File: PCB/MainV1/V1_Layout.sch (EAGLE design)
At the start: 48 parts, among them IC1 AD826N, IC3 AD623R, U2 MB85RC256VPF-G-JNERE2, X1 STEREOJACK

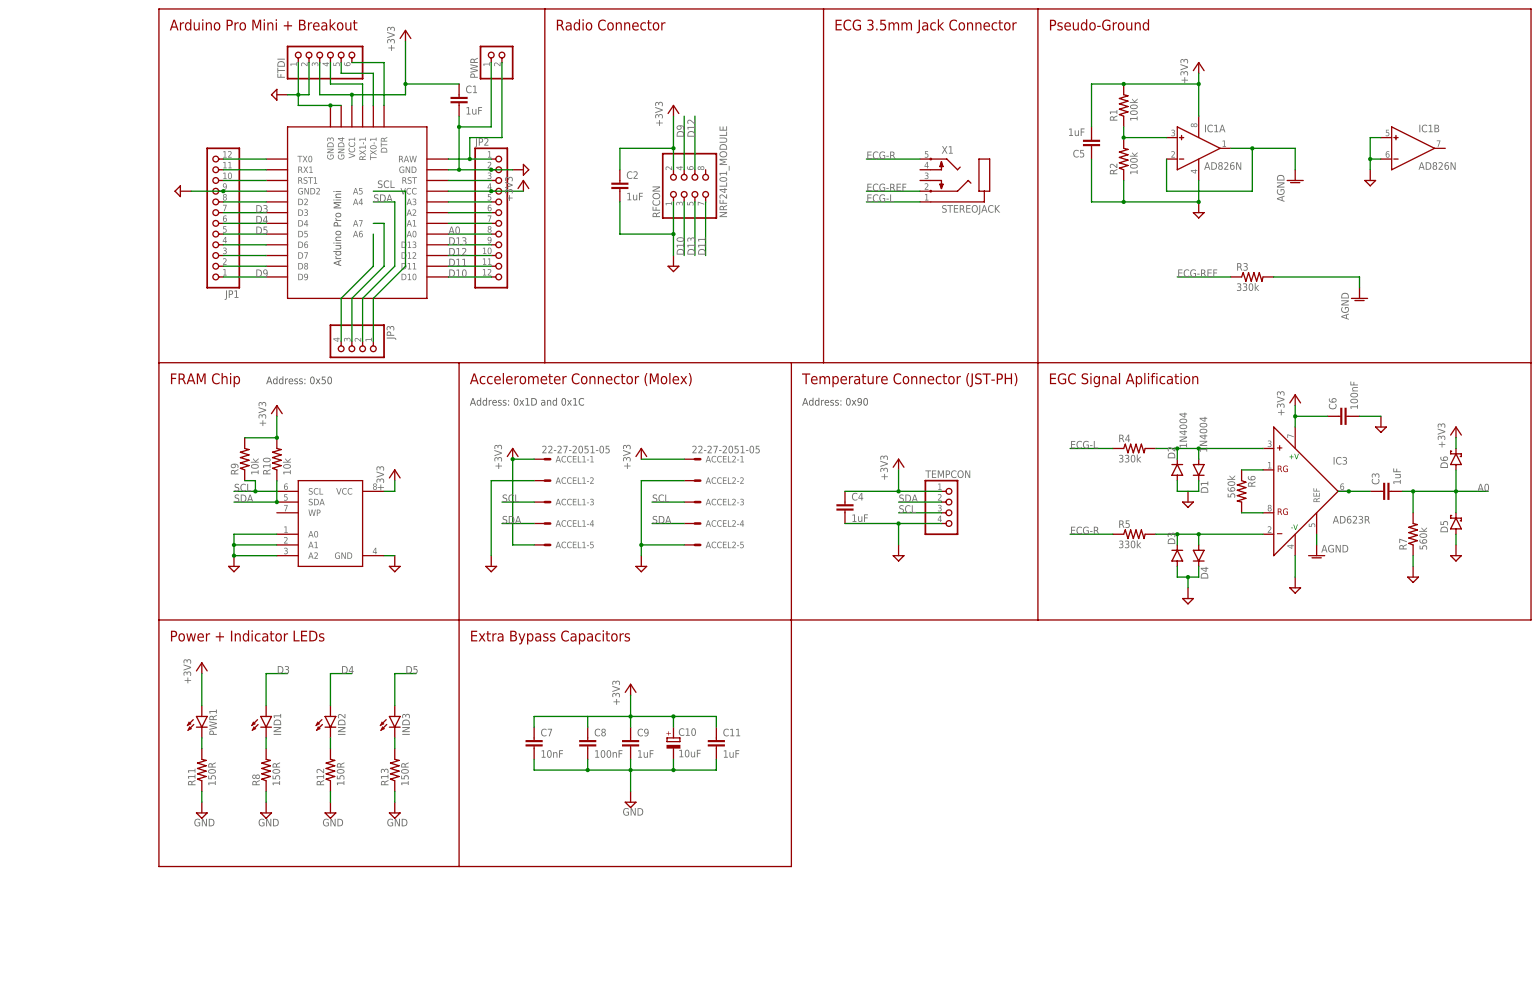
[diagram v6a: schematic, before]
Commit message: started initial main layout. Cleaned up files.
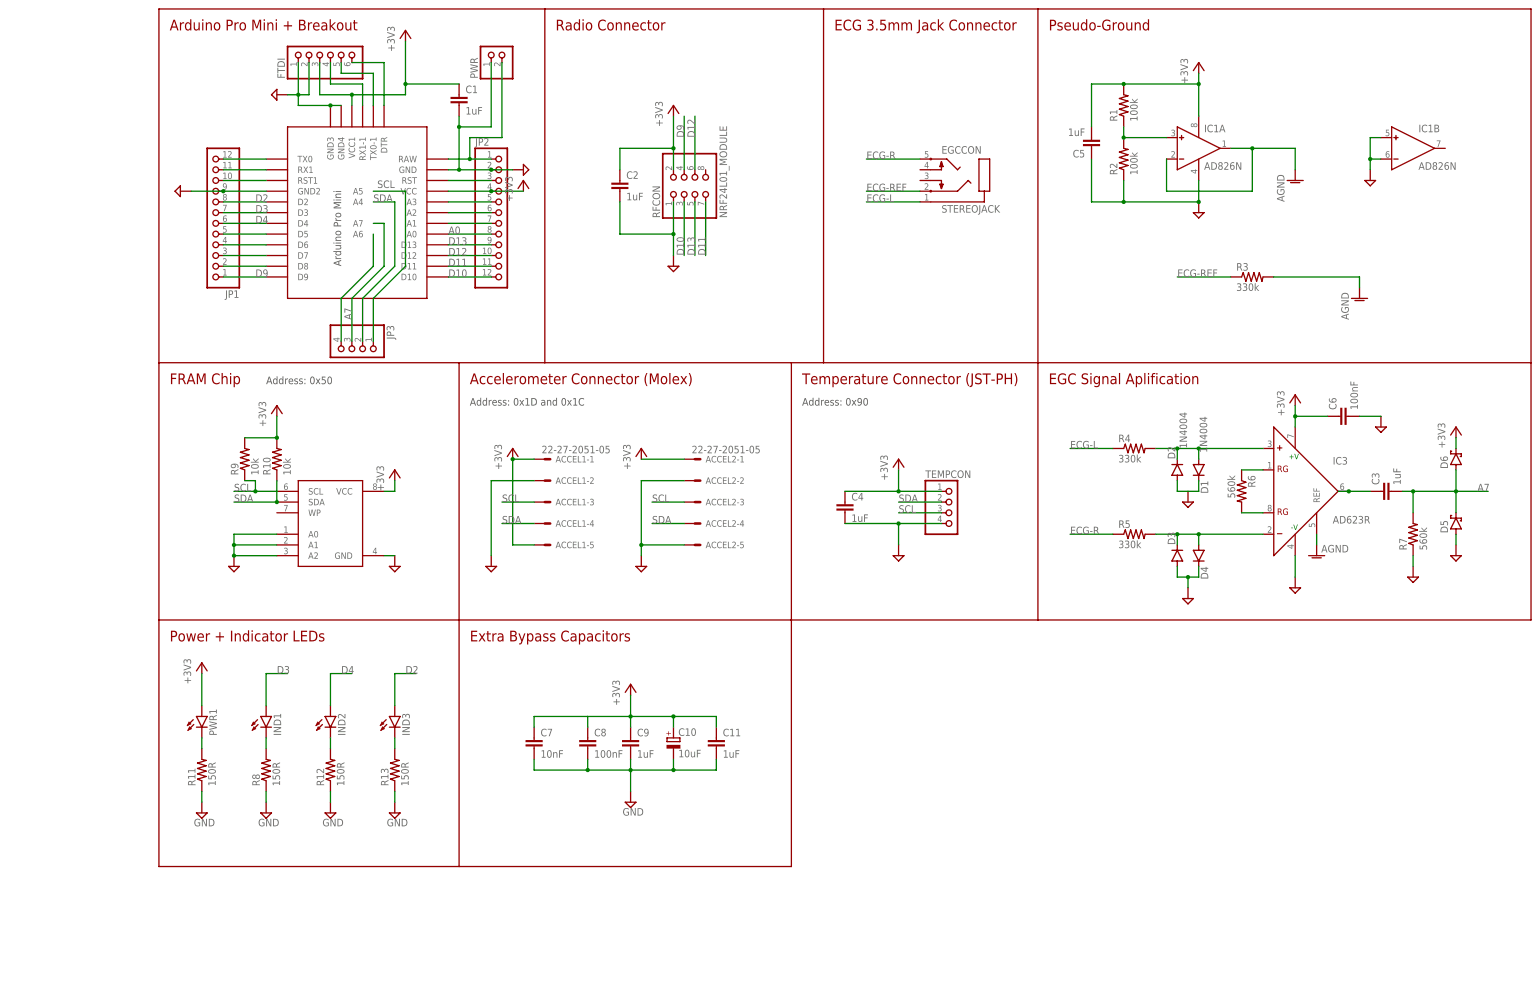
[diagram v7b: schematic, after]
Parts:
- renumbered X1 to EGCCON
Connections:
- removed net N$17: JP1.8, U$1.D2
- removed net N$29: JP3.3, U$1.A7
- new net A7: C3.2, D5.C, D6.A, JP3.3, R7.2, U$1.A7
- new net D2: IND3.A, JP1.8, U$1.D2
- net A0: no longer C3.2, D5.C, D6.A, R7.2
- net D5: no longer IND3.A

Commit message: First draft of completed layout and route
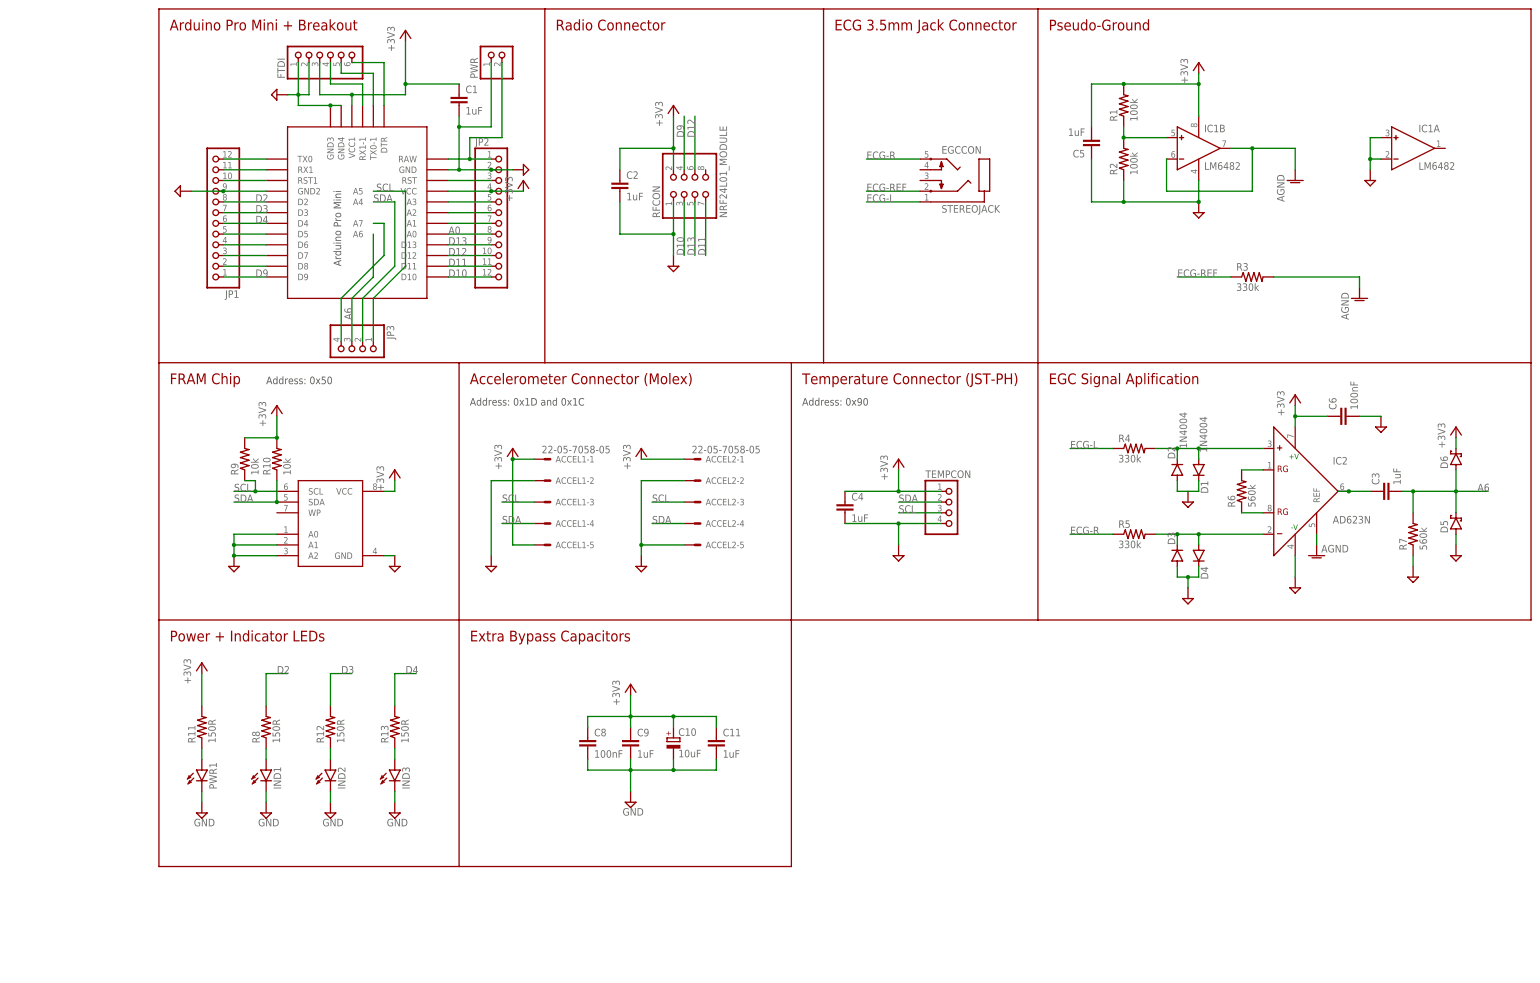
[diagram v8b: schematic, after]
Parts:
- removed C7: 10nF, rcl:C-EUC0603
- removed IC3: AD623R, analog-devices:AD623R
- added IC2: AD623N, analog-devices:AD623N
- ACCEL1, ACCEL2: value 22-27-2051-05 -> 22-05-7058-05; device con-molex:22-27-2051-05 -> con-molex:22-05-7058-05
- C10: device rcl:CPOL-EUE3.5-8 -> rcl:CPOL-EUTAP5-45
- IC1: value AD826N -> LM6482
- R6: device rcl:R-US_R0805 -> rcl:R-US_R0603
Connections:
- removed net A7: C3.2, D5.C, D6.A, JP3.3, R7.2, U$1.A7
- new net A6: C3.2, D5.C, D6.A, JP3.3, R7.2, U$1.A6
- net +3V3: now also IC2.+V, R11.2; no longer C7.1, IC3.+V, PWR1.A
- net AGND: now also IC1B.IN-, IC1B.OUT, IC2.REF; no longer IC1A.IN-, IC1A.OUT, IC3.REF
- net D2: now also R8.2; no longer IND3.A
- net D3: now also R12.2; no longer IND1.A
- net D4: now also R13.2; no longer IND2.A
- net GND: now also IC1A.IN+, IC1A.IN-, IC2.-V, IND1.C, IND2.C, IND3.C, PWR1.C; no longer C7.2, IC1B.IN+, IC1B.IN-, IC3.-V, R11.1, R12.1, R13.1, R8.1
- net N$1: now also PWR1.A, R11.1; no longer PWR1.C, R11.2
- net N$14: now also IND1.A, R8.1; no longer IND1.C, R8.2
- net N$15: now also IND2.A, R12.1; no longer IND2.C, R12.2
- net N$16: now also IND3.A, R13.1; no longer IND3.C, R13.2
- net N$2: now also IC2.-; no longer IC3.-
- net N$28: now also U$1.A7; no longer U$1.A6
- net N$3: now also IC1B.IN+; no longer IC1A.IN+
- net N$5: now also IC2.+; no longer IC3.+
- net N$6: now also IC2.OUT; no longer IC3.OUT
- net N$7: now also IC2.RG@2, R6.1; no longer IC3.RG@2, R6.2
- net N$8: now also IC2.RG@1, R6.2; no longer IC3.RG@1, R6.1
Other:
- moved on the sheet: IC1A, IC1B, IND1, IND2, IND3, PWR1, R11, R12, R13, R6, R8
